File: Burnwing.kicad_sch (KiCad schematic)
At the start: 54 parts, among them J1 Conn_01x02_Pin, J2 USB Type C, J5 Conn_01x06_MountingPin, J6 Conn_01x06_MountingPin, Q1 AONR21307, SW1 SW_DIP_x02, U1 HUSB238, U2 BTS7030-2EPA, U3 TLV73333PDBV

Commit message: fix: Change MCU connector to 1x03
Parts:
- J1: value Conn_01x02_Pin -> Conn_01x03_Pin; footprint Connector_PinHeader_2.54mm:PinHeader_1x02_P2.54mm_Vertical -> Connector_PinHeader_2.54mm:PinHeader_1x03_P2.54mm_Vertical; symbol Connector:Conn_01x02_Pin -> Connector:Conn_01x03_Pin
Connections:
- net GND: now also J1.3 (Pin_3)
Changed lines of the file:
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@@
 	(wire
 		(pts
+			(xy 57.15 191.77) (xy 58.42 191.77)
+		)
+		(stroke
+			(width 0)
+			(type default)
+		)
+	)
+	(wire
+		(pts
 			(xy 38.1 162.56) (xy 40.64 162.56)
 		)
@@
 	)
 	(symbol
-		(lib_id "Connector:Conn_01x02_Pin")
-		(at 52.07 186.69 0)
+		(lib_id "Connector:Conn_01x03_Pin")
+		(at 52.07 189.23 0)
 		(unit 1)
 		(body_style 1)
@@
 		(dnp no)
 		(property "Reference" "J1"
-			(at 53.848 182.372 0)
+			(at 53.848 184.912 0)
 			(show_name no)
 			(do_not_autoplace no)
@@
 			)
 		)
-		(property "Value" "Conn_01x02_Pin"
-			(at 52.705 184.15 0)
+		(property "Value" "Conn_01x03_Pin"
+			(at 52.705 186.69 0)
 			(hide yes)
 			(show_name no)
@@
 			)
 		)
-		(property "Footprint" "Connector_PinHeader_2.54mm:PinHeader_1x02_P2.54mm_Vertical"
-			(at 52.07 186.69 0)
+		(property "Footprint" "Connector_PinHeader_2.54mm:PinHeader_1x03_P2.54mm_Vertical"
+			(at 52.07 189.23 0)
 			(hide yes)
 			(show_name no)
@@
 		)
 		(property "Datasheet" ""
-			(at 52.07 186.69 0)
+			(at 52.07 189.23 0)
 			(hide yes)
 			(show_name no)
@@
 			)
 		)
-		(property "Description" "Generic connector, single row, 01x02, script generated"
-			(at 52.07 186.69 0)
+		(property "Description" "Generic connector, single row, 01x03, script generated"
+			(at 52.07 189.23 0)
 			(hide yes)
 			(show_name no)
@@
 		(pin "2"
 		)
+		(pin "3"
+		)
 		(instances
 			(project "Burnwing"
@@
 					(unit 1)
 				)
+			)
+		)
+	)
+	(symbol
+		(lib_id "power:GND")
+		(at 58.42 191.77 0)
+		(mirror y)
+		(unit 1)
+		(body_style 1)
+		(exclude_from_sim no)
+		(in_bom yes)
+		(on_board yes)
+		(in_pos_files yes)
+		(dnp no)
+		(property "Reference" "#PWR048"
+			(at 58.42 198.12 0)
+			(hide yes)
+			(show_name no)
+			(do_not_autoplace no)
+			(effects
+				(font
+					(size 1.27 1.27)
+				)
+			)
+		)
+		(property "Value" "GND"
+			(at 58.42 195.58 0)
+			(show_name no)
+			(do_not_autoplace no)
+			(effects
+				(font
+					(size 1.27 1.27)
+				)
+			)
+		)
+		(property "Footprint" ""
+			(at 58.42 191.77 0)
+			(hide yes)
+			(show_name no)
+			(do_not_autoplace no)
+			(effects
+				(font
+					(size 1.27 1.27)
+				)
+			)
+		)
+		(property "Datasheet" ""
+			(at 58.42 191.77 0)
+			(hide yes)
+			(show_name no)
+			(do_not_autoplace no)
+			(effects
+				(font
+					(size 1.27 1.27)
+				)
+			)
+		)
+		(property "Description" "Power symbol creates a global label with name \"GND\" , ground"
+			(at 58.42 191.77 0)
+			(hide yes)
+			(show_name no)
+			(do_not_autoplace no)
+			(effects
+				(font
+					(size 1.27 1.27)
+				)
+			)
+		)
+		(pin "1"
+		)
+		(instances
+			(project "Burnwing"
+				(path "/668c3a07-3236-4b27-b3a6-03c249258f7f"
+					(reference "#PWR048")
+					(unit 1)
+				)

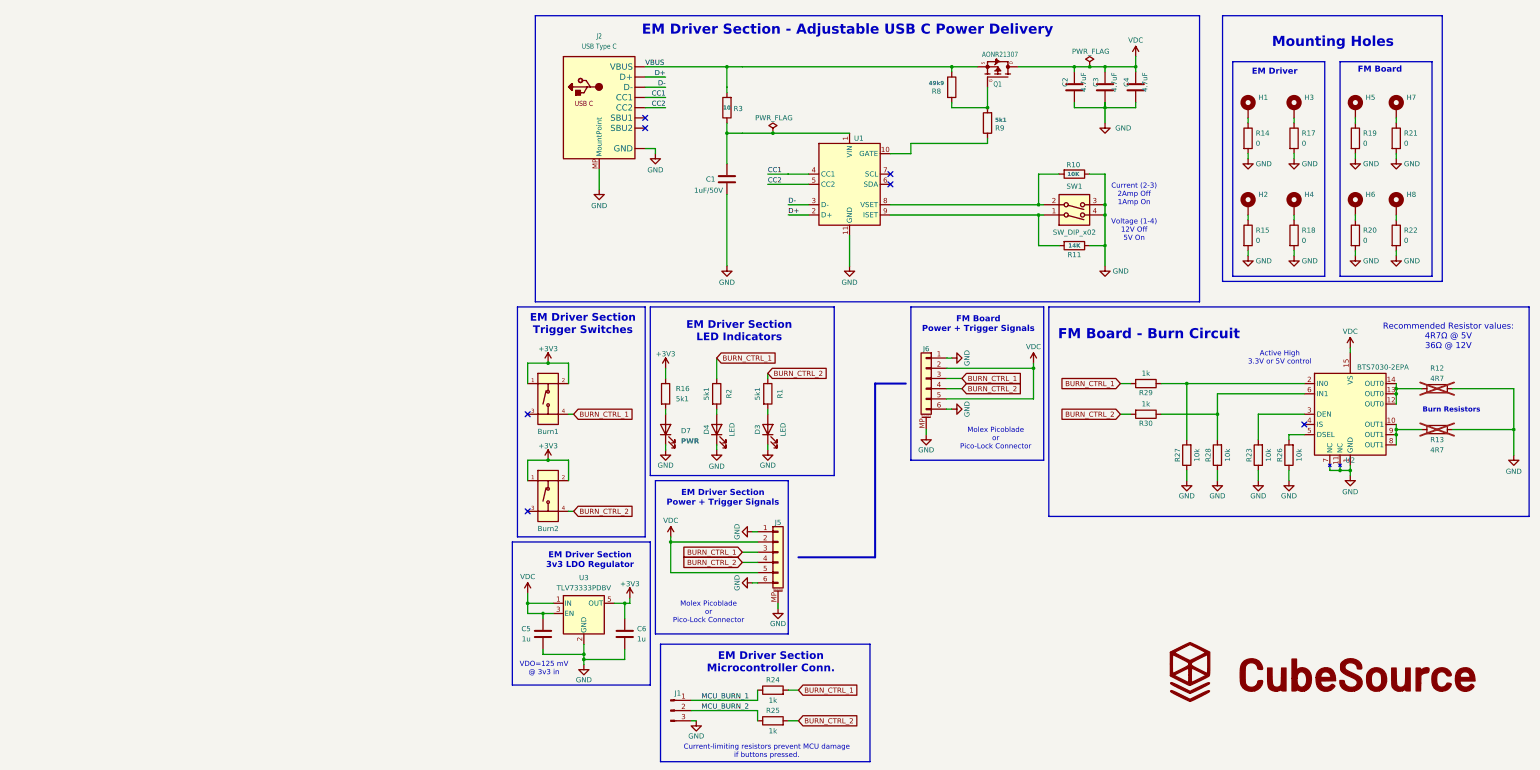
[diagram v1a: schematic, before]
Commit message: fix: Replaced TLV73333 with automotive TPS70933 LDO
- TLV73333 (5.5V max) was too low for 12VDC
- Swapped U3 to TPS70933QDBVRQ1 (C90991): AEC-Q100, 30V in, 150mA, pin-compatible
- Bumped C6 to 4.7uF (C437557) — TPS709 needs >=2.2uF output cap
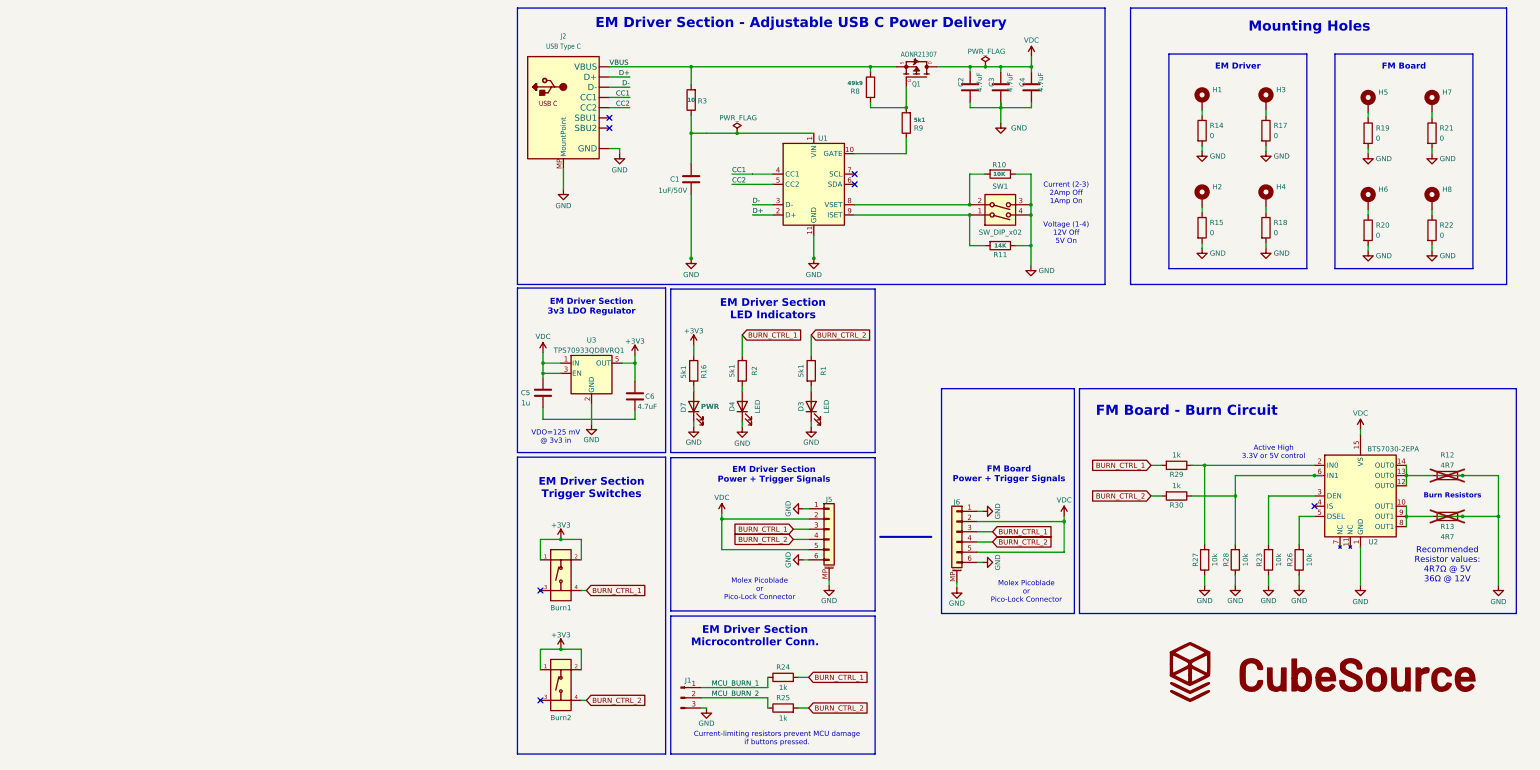
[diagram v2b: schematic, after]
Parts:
- C6: value 1u -> 4.7uF; LCSC (none) -> C437557
- U3: value TLV73333PDBV -> TPS70933QDBVRQ1; symbol Regulator_Linear:TLV73333PDBV -> 00-Project-Symbol-Lib:TPS70933QDBVRQ1; LCSC (none) -> C90991
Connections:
- net GND: no longer C5.2, C6.2, U2.11 (NC), U2.7 (NC)
- new net: C5.2, C6.2
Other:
- moved on the sheet: Burn1, Burn2, C1, C2, C3, C4, C5, C6, D3, D4, D7, H1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

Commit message: fix: Aligned schematic to 50mil grid, removed dangling wires
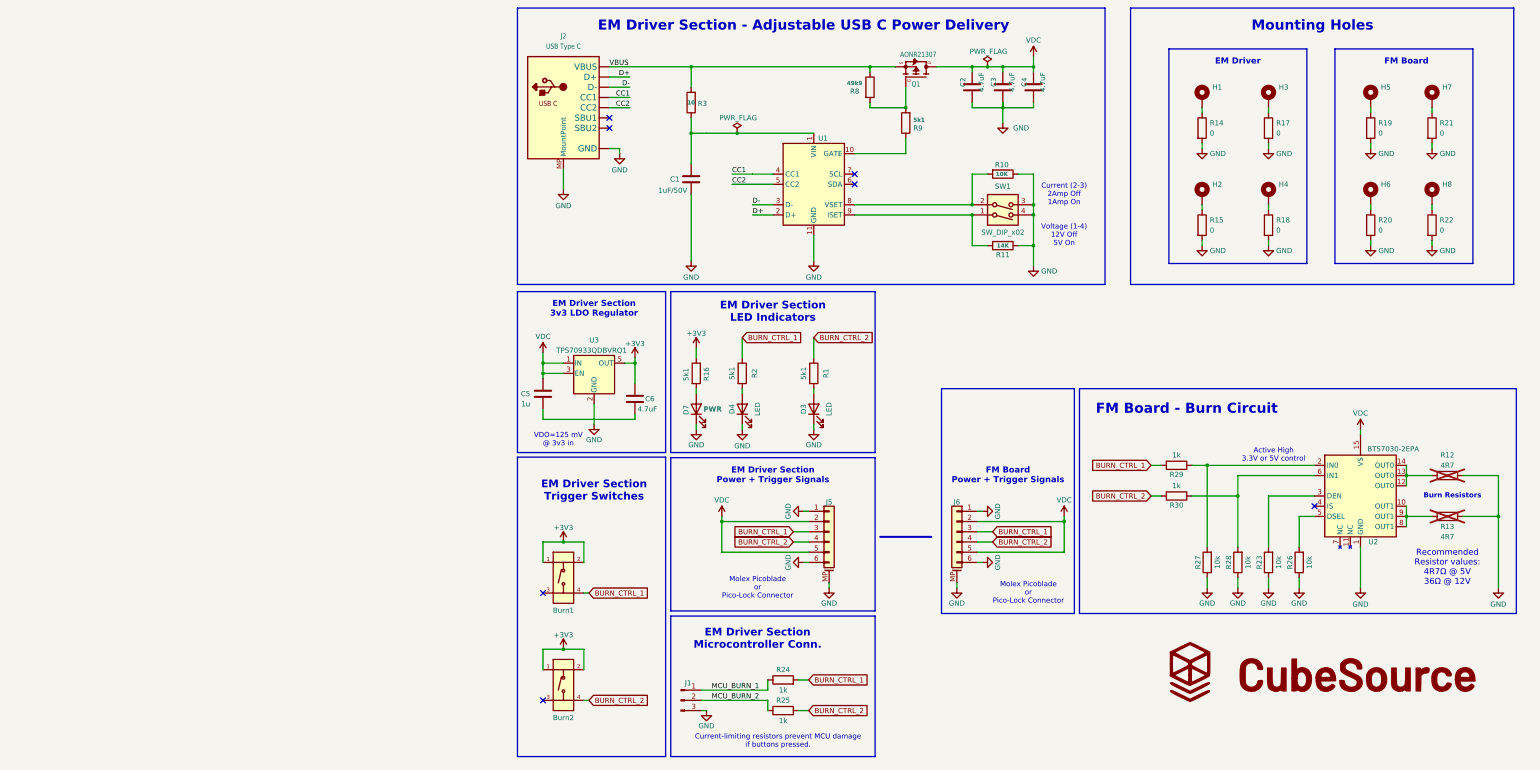
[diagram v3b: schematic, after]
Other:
- moved on the sheet: Burn1, Burn2, C2, C3, C4, C6, D3, D4, D7, H1, H2, H3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

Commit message: layout routing
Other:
- moved on the sheet: D3, D4, D7, R1, R16, R2

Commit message: layout
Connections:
- net BURN_CTRL_1: now also Burn1.3 (C), J5.4 (Pin_4); no longer J5.3 (Pin_3)
- net BURN_CTRL_2: now also Burn2.3 (C), J5.3 (Pin_3); no longer J5.4 (Pin_4)
- no-connect marks 7 -> 5
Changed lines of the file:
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@@
 	)
 	(junction
+		(at 30.48 160.02)
+		(diameter 0)
+		(color 0 0 0 0)
+	)
+	(junction
 		(at 64.77 142.24)
 		(diameter 0)
@@
 	)
 	(junction
+		(at 30.48 186.69)
+		(diameter 0)
+		(color 0 0 0 0)
+	)
+	(junction
 		(at 142.24 29.21)
 		(diameter 0)
@@
 		(at 97.79 55.88)
 	)
-	(no_connect
-		(at 20.32 160.02)
-	)
-	(no_connect
-		(at 20.32 186.69)
-	)
 	(wire
 		(pts
@@
 	(wire
 		(pts
+			(xy 30.48 193.04) (xy 20.32 193.04)
+		)
+		(stroke
+			(width 0)
+			(type default)
+		)
+	)
+	(wire
+		(pts
+			(xy 20.32 160.02) (xy 20.32 166.37)
+		)
+		(stroke
+			(width 0)
+			(type default)
+		)
+	)
+	(wire
+		(pts
 			(xy 181.61 128.27) (xy 212.09 128.27)
 		)
@@
 	(wire
 		(pts
+			(xy 30.48 166.37) (xy 30.48 160.02)
+		)
+		(stroke
+			(width 0)
+			(type default)
+		)
+	)
+	(wire
+		(pts
 			(xy 200.66 135.89) (xy 212.09 135.89)
 		)
@@
 	(wire
 		(pts
+			(xy 30.48 186.69) (xy 30.48 193.04)
+		)
+		(stroke
+			(width 0)
+			(type default)
+		)
+	)
+	(wire
+		(pts
 			(xy 64.77 140.97) (xy 64.77 142.24)
 		)
@@
 	(wire
 		(pts
+			(xy 20.32 166.37) (xy 30.48 166.37)
+		)
+		(stroke
+			(width 0)
+			(type default)
+		)
+	)
+	(wire
+		(pts
 			(xy 132.08 144.78) (xy 128.27 144.78)
 		)
@@
 	(wire
 		(pts
+			(xy 20.32 186.69) (xy 20.32 193.04)
+		)
+		(stroke
+			(width 0)
+			(type default)
+		)
+	)
+	(wire
+		(pts
 			(xy 185.42 156.21) (xy 185.42 158.75)
 		)
@@
 	)
 	(symbol
+		(lib_name "Conn_01x06_MountingPin_1")
+		(lib_id "Connector_Generic_MountingPin:Conn_01x06_MountingPin")
+		(at 91.44 147.32 0)
+		(mirror x)
+		(unit 1)
+		(body_style 1)
+		(exclude_from_sim no)
+		(in_bom yes)
+		(on_board yes)
+		(in_pos_files yes)
+		(dnp no)
+		(property "Reference" "J5"
+			(at 91.186 137.16 0)
+			(show_name no)
+			(do_not_autoplace no)
+			(effects
+				(font
+					(size 1.27 1.27)
+				)
+			)
+		)
+		(property "Value" "Conn_01x06_MountingPin"
+			(at 91.44 156.21 0)
+			(hide yes)
+			(show_name no)
+			(do_not_autoplace no)
+			(effects
+				(font
+					(size 1.27 1.27)
+				)
+			)
+		)
+		(property "Footprint" "00-Project-Footprint-Lib:Molex_Pico-Lock_and_PicoBlade"
+			(at 91.44 147.32 0)
+			(hide yes)
+			(show_name no)
+			(do_not_autoplace no)
+			(effects
+				(font
+					(size 1.27 1.27)
+				)
+			)
+		)
+		(property "Datasheet" ""
+			(at 91.44 147.32 0)
+			(hide yes)
+			(show_name no)
+			(do_not_autoplace no)
+			(effects
+				(font
+					(size 1.27 1.27)
+				)
+			)
+		)
+		(property "Description" "Generic connectable mounting pin connector, single row, 01x06, script generated (kicad-library-utils/schlib/autogen/connector/)"
+			(at 91.44 147.32 0)
+			(hide yes)
+			(show_name no)
+			(do_not_autoplace no)
+			(effects
+				(font
+					(size 1.27 1.27)
+				)
+			)
+		)
+		(pin "MP"
+		)
+		(pin "4"
+		)
+		(pin "5"
+		)
+		(pin "6"
+		)
+		(pin "1"
+		)
+		(pin "3"
+		)
+		(pin "2"
+		)
+		(instances
+			(project "Burnwing"
+				(path "/668c3a07-3236-4b27-b3a6-03c249258f7f"
+					(reference "J5")
+					(unit 1)
+				)
+			)
+		)
+	)
+	(symbol
 		(lib_id "Device:R")
 		(at 110.49 43.18 180)
@@
 					(unit 1)
 				)
-			)
-		)
-	)
-	(symbol
-		(lib_id "Connector_Generic_MountingPin:Conn_01x06_MountingPin")
-		(at 91.44 144.78 0)
-		(unit 1)
-		(body_style 1)
-		(exclude_from_sim no)
-		(in_bom yes)
-		(on_board yes)
-		(in_pos_files yes)
-		(dnp no)
-		(property "Reference" "J5"
-			(at 91.44 137.414 0)
-			(show_name no)
-			(do_not_autoplace no)
-			(effects
-				(font
-					(size 1.27 1.27)
-				)
-			)
-		)
-		(property "Value" "Conn_01x06_MountingPin"
-			(at 91.44 135.89 0)
-			(hide yes)
-			(show_name no)
-			(do_not_autoplace no)
-			(effects
-				(font
-					(size 1.27 1.27)
-				)
-			)
-		)
-		(property "Footprint" "00-Project-Footprint-Lib:Molex_Pico-Lock_and_PicoBlade"
-			(at 91.44 144.78 0)
-			(hide yes)
-			(show_name no)
-			(do_not_autoplace no)
-			(effects
-				(font
-					(size 1.27 1.27)
-				)
-			)
-		)
-		(property "Datasheet" ""
-			(at 91.44 144.78 0)
-			(hide yes)
-			(show_name no)
-			(do_not_autoplace no)
-			(effects
-				(font
-					(size 1.27 1.27)
-				)
-			)
-		)
-		(property "Description" "Generic connectable mounting pin connector, single row, 01x06, script generated (kicad-library-utils/schlib/autogen/connector/)"
-			(at 91.44 144.78 0)
-			(hide yes)
-			(show_name no)
-			(do_not_autoplace no)
-			(effects
-				(font
-					(size 1.27 1.27)
-				)
-			)
-		)
-		(pin "MP"
-		)
-		(pin "4"
-		)
-		(pin "5"
-		)
-		(pin "6"
-		)
-		(pin "1"
-		)
-		(pin "3"
-		)
-		(pin "2"
-		)
-		(instances
-			(project "Burnwing"
-				(path "/668c3a07-3236-4b27-b3a6-03c249258f7f"
-					(reference "J5")
-					(unit 1)
-				)

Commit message: layout stuff
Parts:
- added U4: CH32X035F8U6_C42442062, Library:WQFN-20_L3.0-W3.0-P0.40-TL-EP1.7, symbol Library:CH32X035F8U6_C42442062
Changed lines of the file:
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@@
+	)
+	(symbol
+		(lib_id "Library:CH32X035F8U6_C42442062")
+		(at -67.945 90.17 0)
+		(unit 1)
+		(body_style 1)
+		(exclude_from_sim no)
+		(in_bom yes)
+		(on_board yes)
+		(in_pos_files yes)
+		(dnp no)
+		(fields_autoplaced yes)
+		(property "Reference" "U4"
+			(at -67.945 69.85 0)
+			(show_name no)
+			(do_not_autoplace no)
+			(effects
+				(font
+					(size 1.27 1.27)
+				)
+			)
+		)
+		(property "Value" "CH32X035F8U6_C42442062"
+			(at -67.945 72.39 0)
+			(show_name no)
+			(do_not_autoplace no)
+			(effects
+				(font
+					(size 1.27 1.27)
+				)
+			)
+		)
+		(property "Footprint" "Library:WQFN-20_L3.0-W3.0-P0.40-TL-EP1.7"
+			(at -67.183 116.84 0)
+			(hide yes)
+			(show_name no)
+			(do_not_autoplace no)
+			(effects
+				(font
+					(size 1.27 1.27)
+				)
+			)
+		)
+		(property "Datasheet" "https://www.lcsc.com/datasheet/C42442062.pdf"
+			(at -67.183 119.38 0)
+			(hide yes)
+			(show_name no)
+			(do_not_autoplace no)
+			(effects
+				(font
+					(size 1.27 1.27)
+				)
+			)
+		)
+		(property "Description" ""
+			(at -67.945 90.17 0)
+			(hide yes)
+			(show_name no)
+			(do_not_autoplace no)
+			(effects
+				(font
+					(size 1.27 1.27)
+				)
+			)
+		)
+		(property "Manufacturer" "WCH(南京沁恒)"
+			(at -67.183 121.92 0)
+			(hide yes)
+			(show_name no)
+			(do_not_autoplace no)
+			(effects
+				(font
+					(size 1.27 1.27)
+				)
+			)
+		)
+		(property "MPN" "CH32X035F8U6"
+			(at -67.183 124.46 0)
+			(hide yes)
+			(show_name no)
+			(do_not_autoplace no)
+			(effects
+				(font
+					(size 1.27 1.27)
+				)
+			)
+		)
+		(property "LCSC Part" "C42442062"
+			(at -67.183 127 0)
+			(hide yes)
+			(show_name no)
+			(do_not_autoplace no)
+			(effects
+				(font
+					(size 1.27 1.27)
+				)
+			)
+		)
+		(pin "6"
+		)
+		(pin "12"
+		)
+		(pin "15"
+		)
+		(pin "19"
+		)
+		(pin "7"
+		)
+		(pin "9"
+		)
+		(pin "11"
+		)
+		(pin "4"
+		)
+		(pin "14"
+		)
+		(pin "10"
+		)
+		(pin "20"
+		)
+		(pin "1"
+		)
+		(pin "8"
+		)
+		(pin "2"
+		)
+		(pin "13"
+		)
+		(pin "16"
+		)
+		(pin "3"
+		)
+		(pin "5"
+		)
+		(pin "17"
+		)
+		(pin "18"
+		)
+		(pin "21"
+		)
+		(instances
+			(project "Burnwing"
+				(path "/668c3a07-3236-4b27-b3a6-03c249258f7f"
+					(reference "U4")
+					(unit 1)
+				)
+			)
+		)
 	)
 	(symbol

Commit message: layout
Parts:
- removed U4: CH32X035F8U6_C42442062, Library:WQFN-20_L3.0-W3.0-P0.40-TL-EP1.7, symbol Library:CH32X035F8U6_C42442062
- added J3: Conn_01x02_Pin, symbol Connector:Conn_01x02_Pin
- C5: value 1u -> 1uF
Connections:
- net GND: now also C5.2, C6.2, J3.2 (Pin_2)
- net VDC: no longer U3.3 (EN)
- new net: J3.1 (Pin_1), U3.3 (EN)
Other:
- note removed: "VDO=125 mV @ 3v3 in"
- moved on the sheet: C5, C6, U3
